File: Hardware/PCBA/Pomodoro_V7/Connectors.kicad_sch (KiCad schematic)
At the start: 1 part, among them J4 USB4120-03-C_REVA

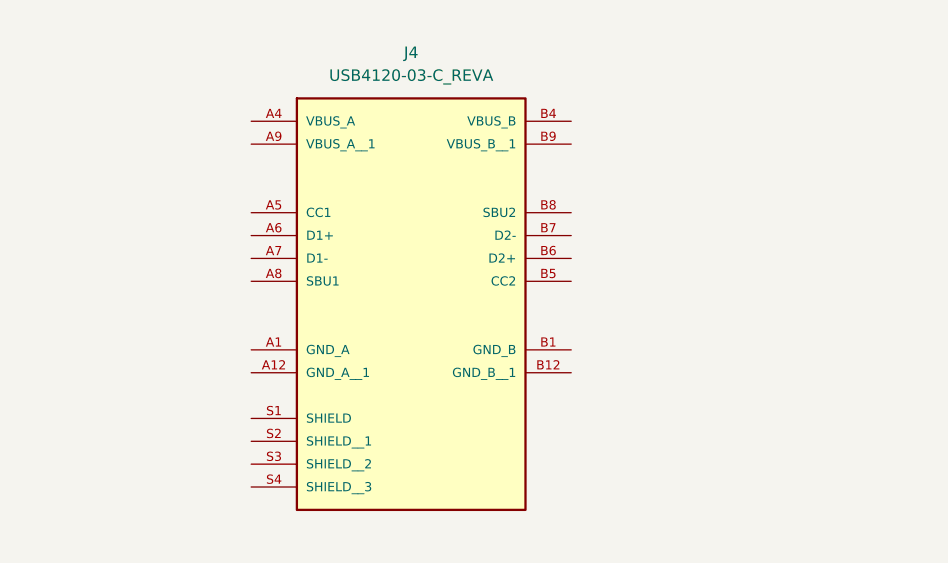
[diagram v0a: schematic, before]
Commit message: Verified the microcontroller Pinout; Added basic peripheral wiring; Added the USBC Wiring
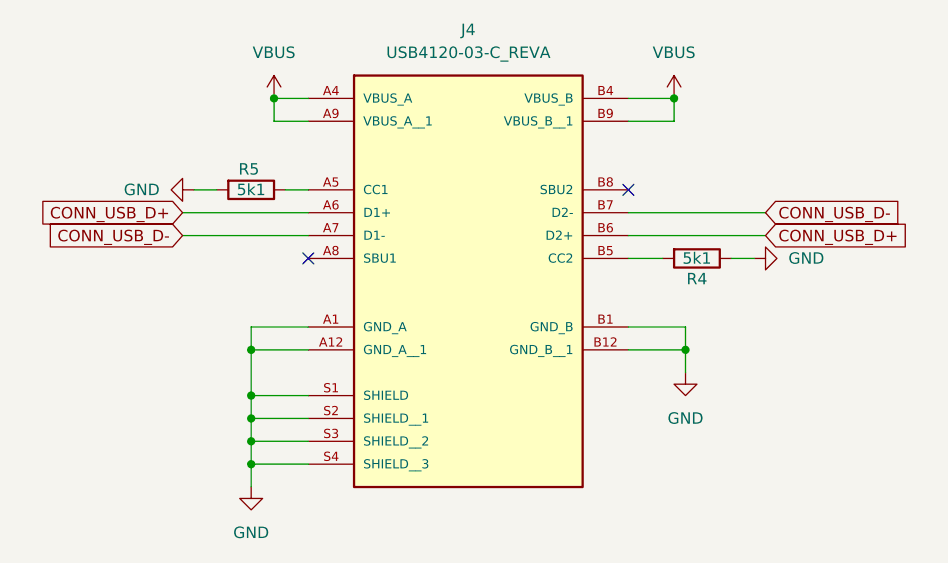
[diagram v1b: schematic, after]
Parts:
- added R4, R5: 5k1, Resistor_SMD:R_0805_2012Metric, symbol Device:R
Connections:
- net GND: now reaches J4.A1 (GND_A)
- net GND: now also J4.A12 (GND_A__1), J4.B1 (GND_B), J4.B12 (GND_B__1), J4.S1 (SHIELD), J4.S2 (SHIELD__1), J4.S3 (SHIELD__2), J4.S4 (SHIELD__3), R4.1, R5.2
- net VBUS: now reaches J4.A4 (VBUS_A)
- net VBUS: now also J4.A9 (VBUS_A__1), J4.B4 (VBUS_B), J4.B9 (VBUS_B__1)
- net at J4.A5 (CC1): now also R5.1
- net CONN_USB_D+: now reaches J4.A6 (D1+)
- net CONN_USB_D+: now also J4.B6 (D2+)
- net CONN_USB_D-: now reaches J4.A7 (D1-)
- net CONN_USB_D-: now also J4.B7 (D2-)
- net at J4.B5 (CC2): now also R4.2
- no-connect marks 0 -> 2
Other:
- moved on the sheet: J4
